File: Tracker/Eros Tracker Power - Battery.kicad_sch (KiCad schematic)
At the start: 16 parts, among them Q1 BSS138, Q1 CJ2305, Q8 CJ2305, U2 TPS62A01A, U5 MCP73834-FCI/MF

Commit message: Midway through board layout
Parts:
- removed D1: SS34, Diode_SMD:D_SMB, symbol Diode:B220
- removed Q1 (x2): BSS138, Package_TO_SOT_SMD:SOT-23, symbol Transistor_FET:BSS138
- removed Q1, Q8: CJ2305, Package_TO_SOT_SMD:SOT-23, symbol Transistor_FET:AO3401A
- added D2: SS34FA, Eros Tracker:SODFL3618X143N, symbol Eros Tracker:SS34FA
- added Q4: DMP2240UDM-7, Eros Tracker:SOT95P285X140-6N, symbol Eros Tracker:DMP2240UDM-7
- added Q5, Q6: DMC1028UVT-7, Eros Tracker:SOT95P285X140-6N, symbol Eros Tracker:DMC1028UVT-7
- added R15, R16: 10k 1%, Resistor_SMD:R_0805_2012Metric, symbol Device:R_US
- C2: footprint (none) -> Capacitor_SMD:C_0805_2012Metric; Manufacturer_Name (none) -> Murata; Manufacturer_Part_Number (none) -> GRM21BR71C475KE51L; Mouser Part Number (none) -> 81-GRM21BR71C475KE1L; Mouser Price/Stock (none) -> https://www.mouser.com/ProductDetail/Murata-Electronics/GRM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
- C3: renamed from C1; footprint (none) -> Capacitor_SMD:C_0805_2012Metric; Manufacturer_Name (none) -> Murata; Manufacturer_Part_Number (none) -> GRM21BZ70J226ME44L; Mouser Part Number (none) -> 81-GRM21BZ70J226ME4L; Mouser Price/Stock (none) -> https://www.mouser.com/ProductDetail/Murata-Electronics/GRM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
- L1: footprint (none) -> Eros Tracker:DFE2HCAH1R0MJ0L; Height (none) -> 1.3; Manufacturer_Name (none) -> Murata; Manufacturer_Part_Number (none) -> DFE252012F-1R0M=P2; Mouser Part Number (none) -> 81-DFE252012F-1R0MP2; Mouser Price/Stock (none) -> https://www.mouser.com/ProductDetail/Murata-Electronics/DFE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
- R11: renamed from R4; value 10k -> 10k 1%; footprint (none) -> Resistor_SMD:R_0805_2012Metric; Manufacturer_Name (none) -> YAGEO; Manufacturer_Part_Number (none) -> RT0805FRE0710KL; Mouser Part Number (none) -> 603-RT0805FRE0710KL; Mouser Price/Stock (none) -> https://www.mouser.com/ProductDetail/YAGEO/RT0805FRE0710KL?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
- R12: renamed from R1; value 10k -> 10k 1%; footprint (none) -> Resistor_SMD:R_0805_2012Metric; Manufacturer_Name (none) -> YAGEO; Manufacturer_Part_Number (none) -> RT0805FRE0710KL; Mouser Part Number (none) -> 603-RT0805FRE0710KL; Mouser Price/Stock (none) -> https://www.mouser.com/ProductDetail/YAGEO/RT0805FRE0710KL?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
- R13: renamed from R5; value R_US -> 45k3 1%; footprint (none) -> Resistor_SMD:R_0805_2012Metric; Manufacturer_Name (none) -> YAGEO; Manufacturer_Part_Number (none) -> RT0805DRE0745K3L; Mouser Part Number (none) -> 603-RT0805DRE0745K3L; Mouser Price/Stock (none) -> https://www.mouser.com/ProductDetail/YAGEO/RT0805DRE0745K3L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
- R14: renamed from R6; value R_US -> 10k 1%; footprint (none) -> Resistor_SMD:R_0805_2012Metric; Manufacturer_Name (none) -> YAGEO; Manufacturer_Part_Number (none) -> RT0805FRE0710KL; Mouser Part Number (none) -> 603-RT0805FRE0710KL; Mouser Price/Stock (none) -> https://www.mouser.com/ProductDetail/YAGEO/RT0805FRE0710KL?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
- R17: renamed from R3; value 833 -> 835R; footprint (none) -> Resistor_SMD:R_0805_2012Metric; Manufacturer_Name (none) -> YAGEO; Manufacturer_Part_Number (none) -> RT0805BRD07835RL; Mouser Part Number (none) -> 603-RT0805BRD07835RL; Mouser Price/Stock (none) -> https://www.mouser.com/ProductDetail/YAGEO/RT0805BRD07835RL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
- R18: renamed from R2; value 10k -> 10k 1%; footprint (none) -> Resistor_SMD:R_0805_2012Metric; Manufacturer_Name (none) -> YAGEO; Manufacturer_Part_Number (none) -> RT0805FRE0710KL; Mouser Part Number (none) -> 603-RT0805FRE0710KL; Mouser Price/Stock (none) -> https://www.mouser.com/ProductDetail/YAGEO/RT0805FRE0710KL?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
- U2: footprint Eros Tracker:SOT-563 -> Eros Tracker:TPS62A0xA-SOT-563; Manufacturer_Name (none) -> Texas Instruments; Manufacturer_Part_Number (none) -> TPS62A01ADRLR; Mouser Part Number (none) -> 595-TPS62A01ADRLR; Mouser Price/Stock (none) -> https://www.mouser.com/ProductDetail/Texas-Instruments/TPS6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
- U3: renamed from U5; footprint DFN10_3x3MC_MCH -> Eros Tracker:MCP73834-FCI-MF; Manufacturer_Name (none) -> Microchip; Manufacturer_Part_Number (none) -> MCP73834T-FCI/MF; Mouser Part Number (none) -> 579-MCP73834T-FCI/MF; Mouser Price/Stock (none) -> https://www.mouser.com/ProductDetail/Microchip-Technology/M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
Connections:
- net +BATT: now also Q4.6 (D1)
- net GND: now also Q5.5 (S1), Q6.5 (S1), R16.2
- net VBUS: now also D2.2 (A), Q4.1 (G1), Q4.4 (D2), Q5.4 (D2), Q6.4 (D2), R15.1
- net VBUS_OUT: now also Q4.2 (S2)
- net VIN: now also D2.1 (K), Q4.5 (S1)
- net ~{BAT_STAT_CHRG_DONE}: now also Q4.3 (G2)
- new net POWER_VIN1: Q5.2 (S2), Q5.6 (D1), Q6.1 (G1), Q6.3 (G2), R15.2
- new net POWER_VIN2: Q5.1 (G1), Q5.3 (G2), Q6.2 (S2), Q6.6 (D1), R16.1
- no-connect marks 0 -> 1
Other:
- note removed: "+"
- note removed: "-"

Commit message: Alpha release
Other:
- note added: "Place as close as possible to battery connection"
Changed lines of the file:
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@@
     (stroke (width 0) (type default))
   )
-  (wire (pts (xy 73.66 204.47) (xy 81.28 204.47))
+  (wire (pts (xy 74.93 204.47) (xy 81.28 204.47))
     (stroke (width 0) (type default))
   )
@@
     (effects (font (size 1.27 1.27)) (justify left bottom))
   )
+  (text "Place as close as possible to battery connection\n" (at 229.87 43.18 0)
+    (effects (font (size 1.27 1.27)) (justify left bottom))
+  )
   (text "R5, R6 0805, 1%" (at 123.19 86.36 0)
     (effects (font (size 1.27 1.27)) (justify left bottom))
@@
     (effects (font (size 1.27 1.27)) (justify right))
   )
-  (hierarchical_label "VBUS" (shape input) (at 73.66 204.47 0) (fields_autoplaced)
-    (effects (font (size 1.27 1.27)) (justify left))
+  (hierarchical_label "VBUS" (shape input) (at 74.93 204.47 180) (fields_autoplaced)
+    (effects (font (size 1.27 1.27)) (justify right))
   )
   (hierarchical_label "VBUS" (shape input) (at 232.41 144.78 180) (fields_autoplaced)

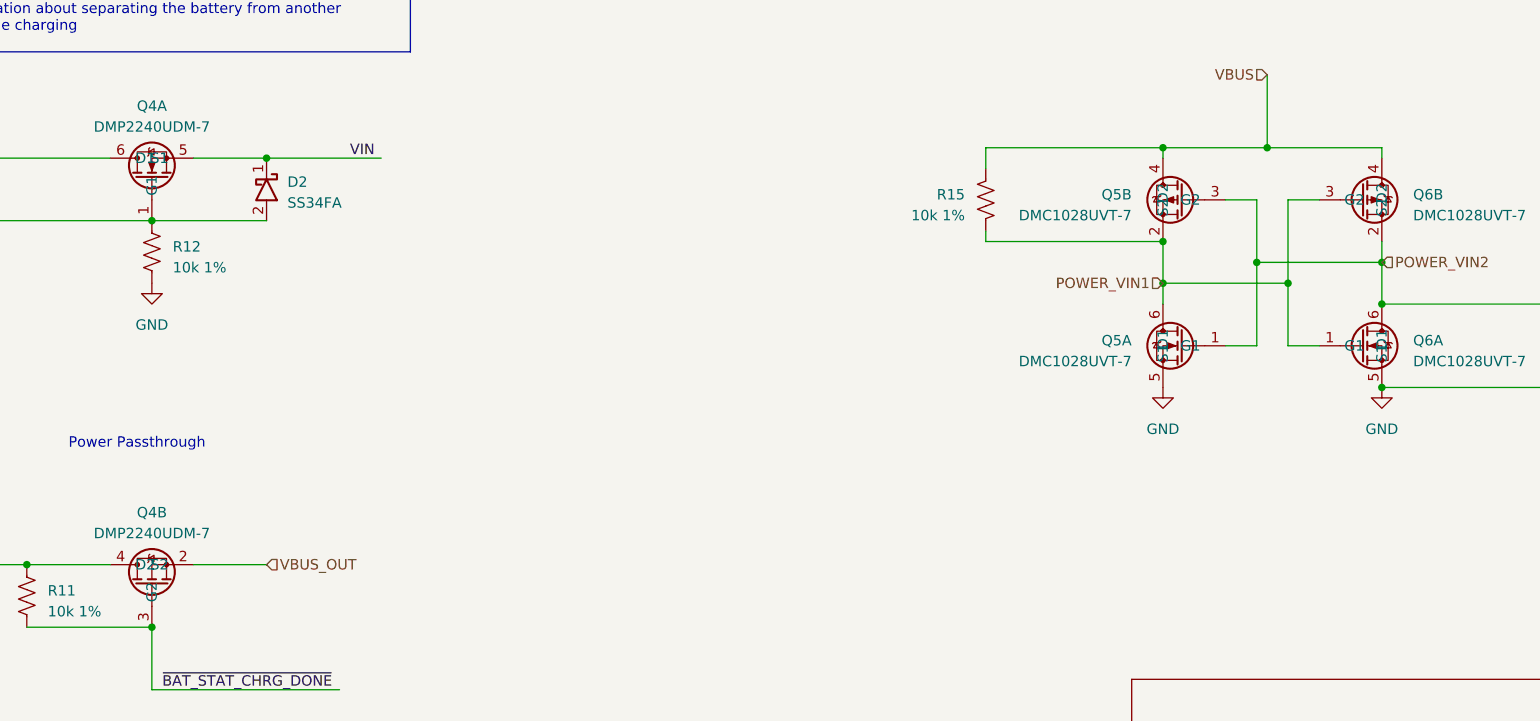
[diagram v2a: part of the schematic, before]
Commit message: Added cuts and jumps for Rev A
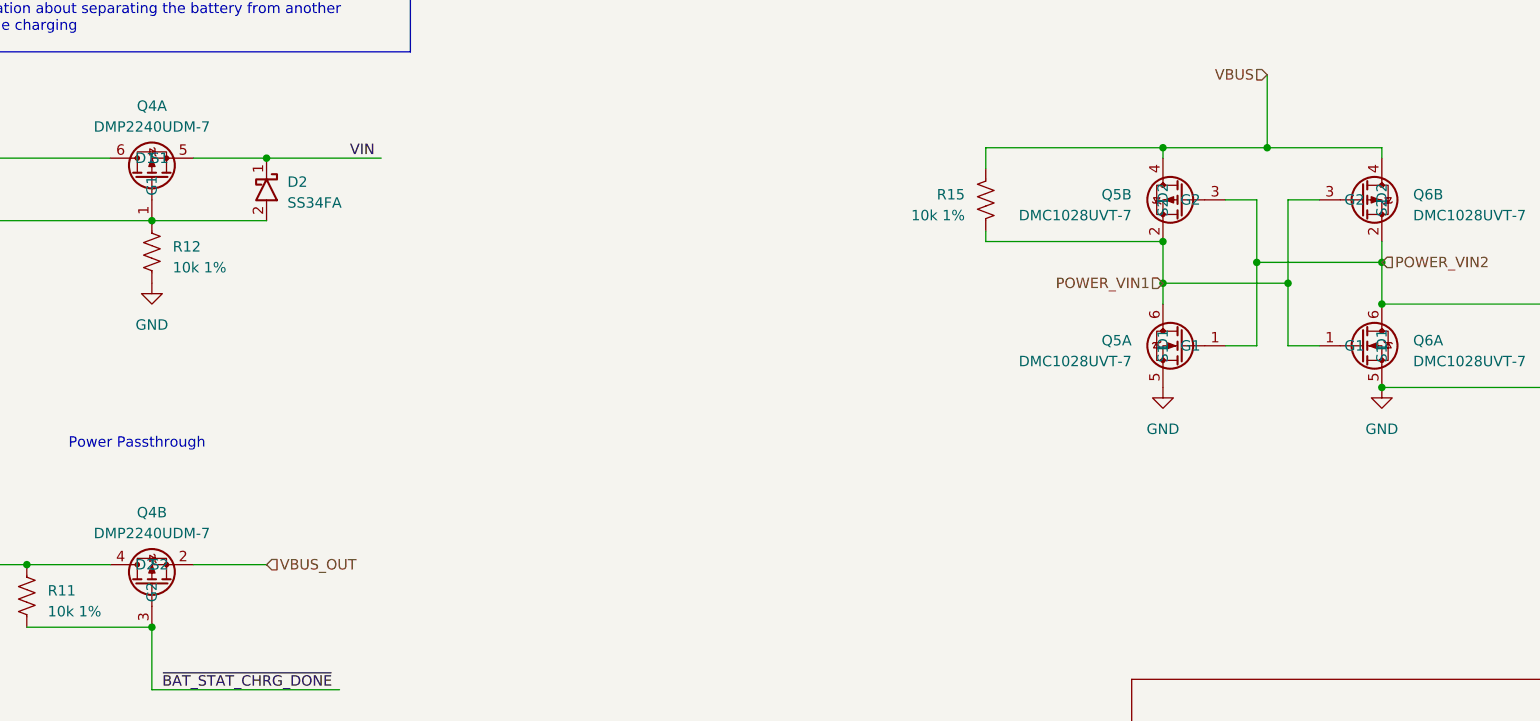
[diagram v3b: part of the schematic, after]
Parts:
- D2: footprint Eros Tracker:SODFL3618X143N -> SODFL3618X143N
- Q4: footprint Eros Tracker:SOT95P285X140-6N -> SOT95P285X140-6N
- Q5, Q6: footprint Eros Tracker:SOT95P285X140-6N -> SOT95P280X100-6N
- U2: footprint Eros Tracker:TPS62A0xA-SOT-563 -> Eros Tracker:SOT-563
- U3: footprint Eros Tracker:MCP73834-FCI-MF -> DFN10_3x3MC_MCH
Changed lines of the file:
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@@
       (effects (font (size 1.27 1.27)) hide)
     )
-    (property "Datasheet" "https://www.mouser.com/datasheet/2/447/PYu_RT_1_to_0_01_RoHS_L_12-3003070.pdf" (at 276.86 72.39 0)
+    (property "Datasheet" "~" (at 276.86 72.39 0)
       (effects (font (size 1.27 1.27)) hide)
     )
@@
       (effects (font (size 1.524 1.524)))
     )
-    (property "Footprint" "Eros Tracker:MCP73834-FCI-MF" (at 252.73 49.784 0)
+    (property "Footprint" "DFN10_3x3MC_MCH" (at 252.73 49.784 0)
       (effects (font (size 1.524 1.524)) hide)
     )
@@
       (effects (font (size 1.27 1.27)) hide)
     )
-    (property "Datasheet" "https://www.mouser.com/datasheet/2/447/PYu_RT_1_to_0_01_RoHS_L_12-3003070.pdf" (at 96.52 166.37 0)
+    (property "Datasheet" "~" (at 96.52 166.37 0)
       (effects (font (size 1.27 1.27)) hide)
     )
@@
       (effects (font (size 1.27 1.27)) hide)
     )
-    (property "Datasheet" "https://www.mouser.com/datasheet/2/281/1/GRM21BR71C475KE51_01A-1986969.pdf" (at 58.42 62.23 0)
+    (property "Datasheet" "~" (at 58.42 62.23 0)
       (effects (font (size 1.27 1.27)) hide)
     )
@@
       (effects (font (size 1.27 1.27)) (justify left))
     )
-    (property "Footprint" "Eros Tracker:SOT95P285X140-6N" (at 200.66 254.94 0)
+    (property "Footprint" "SOT95P280X100-6N" (at 200.66 254.94 0)
       (effects (font (size 1.27 1.27)) (justify left top) hide)
     )
@@
       (effects (font (size 1.27 1.27)) hide)
     )
-    (property "Datasheet" "https://www.mouser.com/datasheet/2/447/PYu_RT_1_to_0_01_RoHS_L_12-3003070.pdf" (at 81.28 208.28 0)
+    (property "Datasheet" "~" (at 81.28 208.28 0)
       (effects (font (size 1.27 1.27)) hide)
     )
@@
       (effects (font (size 1.27 1.27)) (justify left))
     )
-    (property "Footprint" "Eros Tracker:SOT95P285X140-6N" (at 265.43 254.94 0)
+    (property "Footprint" "SOT95P280X100-6N" (at 265.43 254.94 0)
       (effects (font (size 1.27 1.27)) (justify left top) hide)
     )
@@
       (effects (font (size 1.27 1.27)) hide)
     )
-    (property "Datasheet" "https://www.mouser.com/datasheet/2/447/PYu_RT_1_to_0_01_RoHS_L_12-3003070.pdf" (at 294.64 67.31 0)
+    (property "Datasheet" "~" (at 294.64 67.31 0)
       (effects (font (size 1.27 1.27)) hide)
     )
@@
       (effects (font (size 1.27 1.27)))
     )
-    (property "Footprint" "Eros Tracker:SOT95P285X140-6N" (at 191.44 185.42 0)
+    (property "Footprint" "SOT95P285X140-6N" (at 191.44 185.42 0)
       (effects (font (size 1.27 1.27)) (justify left top) hide)
     )
@@
       (effects (font (size 1.27 1.27)) hide)
     )
-    (property "Datasheet" "https://www.mouser.com/datasheet/2/281/1/GRM21BZ70J226ME44_01A-1987068.pdf" (at 146.05 63.5 0)
+    (property "Datasheet" "~" (at 146.05 63.5 0)
       (effects (font (size 1.27 1.27)) hide)
     )
@@
     )
   )
-  (symbol (lib_name "SS34FA_1") (lib_id "Eros Tracker:SS34FA") (at 110.49 152.4 270) (unit 1)
+  (symbol (lib_id "Eros Tracker:SS34FA") (at 110.49 152.4 270) (unit 1)
     (in_bom yes) (on_board yes) (dnp no) (fields_autoplaced)
     (property "Reference" "D2" (at 113.03 157.8483 90)
@@
       (effects (font (size 1.27 1.27)) (justify left))
     )
-    (property "Footprint" "Eros Tracker:SODFL3618X143N" (at 16.84 165.1 0)
+    (property "Footprint" "SODFL3618X143N" (at 16.84 165.1 0)
       (effects (font (size 1.27 1.27)) (justify left top) hide)
     )
@@
       (effects (font (size 1.27 1.27)) hide)
     )
-    (property "Datasheet" "https://www.mouser.com/datasheet/2/281/1/J_E_TE243A_0017-3158849.pdf" (at 115.57 55.88 0)
+    (property "Datasheet" "~" (at 115.57 55.88 0)
       (effects (font (size 1.27 1.27)) hide)
     )
@@
       (effects (font (size 1.27 1.27)) hide)
     )
-    (property "Datasheet" "https://www.mouser.com/datasheet/2/447/PYu_RT_1_to_0_01_RoHS_L_12-3003070.pdf" (at 129.54 59.69 0)
+    (property "Datasheet" "~" (at 129.54 59.69 0)
       (effects (font (size 1.27 1.27)) hide)
     )
@@
       (effects (font (size 1.27 1.27)) hide)
     )
-    (property "Datasheet" "https://www.mouser.com/datasheet/2/447/PYu_RT_1_to_0_01_RoHS_L_12-3003070.pdf" (at 198.12 160.02 0)
+    (property "Datasheet" "~" (at 198.12 160.02 0)
       (effects (font (size 1.27 1.27)) hide)
     )
@@
       (effects (font (size 1.27 1.27)) hide)
     )
-    (property "Datasheet" "https://www.mouser.com/datasheet/2/447/PYu_RT_1_to_0_01_RoHS_L_12-3003070.pdf" (at 129.54 67.31 0)
+    (property "Datasheet" "~" (at 129.54 67.31 0)
       (effects (font (size 1.27 1.27)) hide)
     )
@@
       (effects (font (size 2.0828 1.7703)) (justify left bottom))
     )
-    (property "Footprint" "Eros Tracker:TPS62A0xA-SOT-563" (at 93.98 60.96 0)
+    (property "Footprint" "Eros Tracker:SOT-563" (at 93.98 60.96 0)
       (effects (font (size 1.27 1.27)) hide)
     )
@@
       (effects (font (size 1.27 1.27)))
     )
-    (property "Footprint" "Eros Tracker:SOT95P285X140-6N" (at 191.44 135.89 0)
+    (property "Footprint" "SOT95P285X140-6N" (at 191.44 135.89 0)
       (effects (font (size 1.27 1.27)) (justify left top) hide)
     )
@@
       (effects (font (size 1.27 1.27)) (justify left))
     )
-    (property "Footprint" "Eros Tracker:SOT95P285X140-6N" (at 265.43 272.72 0)
+    (property "Footprint" "SOT95P280X100-6N" (at 265.43 272.72 0)
       (effects (font (size 1.27 1.27)) (justify left top) hide)
     )
@@
       (effects (font (size 1.27 1.27)) hide)
     )
-    (property "Datasheet" "https://www.mouser.com/datasheet/2/447/PYu_RT_1_to_0_01_RoHS_L_12-3003070.pdf" (at 267.97 177.8 0)
+    (property "Datasheet" "~" (at 267.97 177.8 0)
       (effects (font (size 1.27 1.27)) hide)
     )
@@
       (effects (font (size 1.27 1.27)) (justify left))
     )
-    (property "Footprint" "Eros Tracker:SOT95P285X140-6N" (at 200.66 272.72 0)
-      (effects (font (size 1.27 1.27)) (justify left top) hide)
-    )
+    (property "Footprint" "SOT95P280X100-6N" (at 200.66 272.72 0)
+      (effects (font (size 1.27 1.27)) (justify left top) hide)
+    )
